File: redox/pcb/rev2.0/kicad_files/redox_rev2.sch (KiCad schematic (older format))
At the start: 144 parts, among them J1 AVR-ISP-6, J2 OLED-SSD1306, K1 KEYSW, K10 KEYSW, K11 KEYSW, K12 KEYSW, K13 KEYSW, K14 KEYSW, K15 KEYSW, K16 KEYSW, K17 KEYSW, K18 KEYSW, K19 KEYSW, K2 KEYSW, K20 KEYSW, K21 KEYSW, K22 KEYSW, K23 KEYSW, K24 KEYSW, K25 KEYSW, K26 KEYSW, K27 KEYSW, K28 KEYSW, K29 KEYSW, K3 KEYSW, K30 KEYSW, K31 KEYSW, K32 KEYSW, K33 KEYSW, K34 KEYSW, K35 KEYSW, K4 KEYSW, K5 KEYSW, K6 KEYSW, K7 KEYSW, K8 KEYSW, K9 KEYSW, Q1 2N7002, U1 PRTR5V0U2X, U2 ATmega32U4-MU, Y1 16Mhz

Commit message: PCB Routing in progress
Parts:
- added USB2: HRO-TYPE-C-31-M-12, Keebio-Parts:HRO-TYPE-C-31-M-12-Assembly, symbol Type-C:HRO-TYPE-C-31-M-12
- C5: footprint Keebio-Parts:C_0603 -> Capacitor_Tantalum_SMD:CP_EIA-3216-12_Kemet-S_Pad1.58x1.35mm_HandSolder; symbol Device:C_Small -> Device:CP1
- D1, D10, D11, D12, D13, D14, D15, D16, D17, D18, D19, D2, D20, D21, D22, D23, D24, D25, D26, D27, D28, D29, D3, D30, D31, D32, D33, D34, D35, D4, D5, D6, D7, D8, D9: footprint redox_footprints:Diode_SOD123 -> redox_footprints:D_0805_dualsided
- F1: footprint Keebio-Parts:Fuse_0805 -> Fuse:Fuse_1206_3216Metric_Pad1.42x1.75mm_HandSolder
- K11: footprint redox_footprints:Mx_Alps_125-dualside_with_LED -> redox_footprints:Mx_Alps_100-dualside_with_LED
- R10, R11, R12, R13, R14, R15, R16, R17, R18, R19, R20, R21, R22, R23, R24, R25, R26, R27, R28, R29, R30, R31, R32, R33, R34, R35, R36, R37, R38, R39, R40, R41, R42, R43, R44: footprint Keebio-Parts:Resistor-Compact -> redox_footprints:R_0805_dualsided
- U2: value ATmega32U4-MU -> ATmega32U4; symbol Voyager60-rescue:ATmega32U4-MU-MCU_Microchip_ATmega -> ATmega32U4:ATMEGA32U4
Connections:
- net labels added: XTAL1, XTAL2
- wire segments 509 -> 505
- no-connect marks 8 -> 10
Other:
- moved on the sheet: C1, C2, C3, C4, C6, C7, F1, H1, H2, H3, H4, J1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

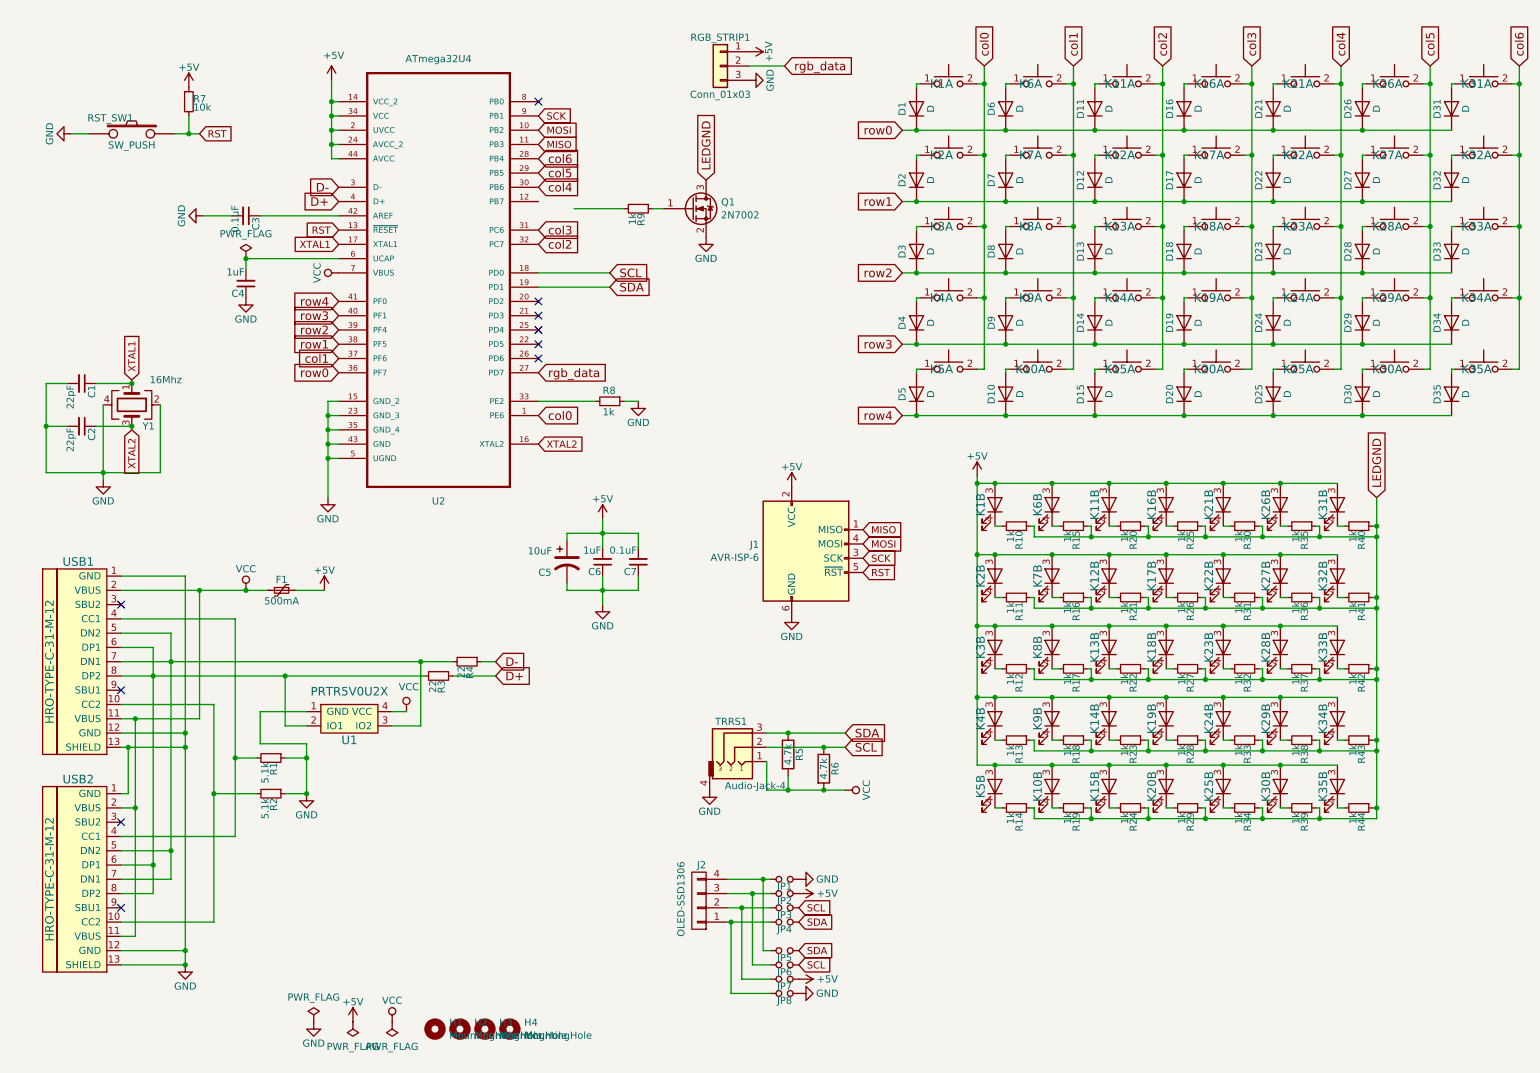
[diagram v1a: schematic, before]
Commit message: Create dual sided usb
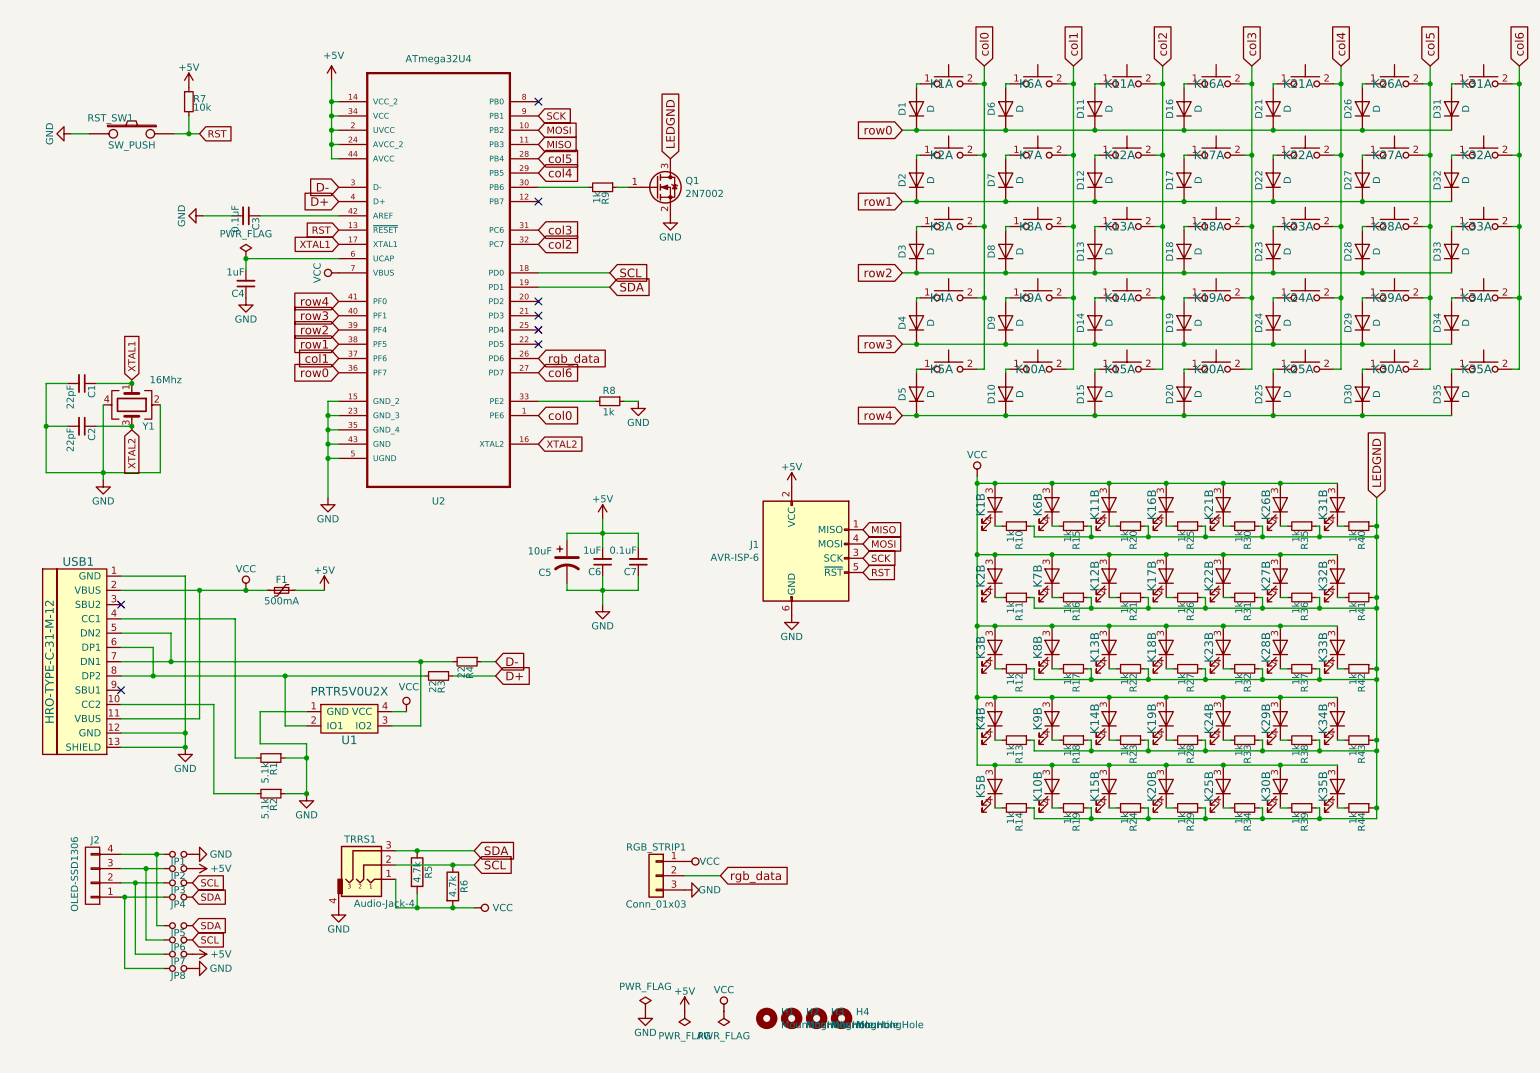
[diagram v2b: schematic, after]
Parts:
- removed USB2: HRO-TYPE-C-31-M-12, Keebio-Parts:HRO-TYPE-C-31-M-12-Assembly, symbol Type-C:HRO-TYPE-C-31-M-12
- USB1: footprint Keebio-Parts:HRO-TYPE-C-31-M-12-Assembly -> redox_footprints:HRO-TYPE-C-31-M-12-Assembly_dualsided
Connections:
- net +5V: no longer K1.3, K10.3, K11.3, K12.3, K13.3, K14.3, K15.3, K16.3, K17.3, K18.3, K19.3, K2.3, K20.3, K21.3, K22.3, K23.3, K24.3, K25.3, K26.3, K27.3, K28.3, K29.3, K3.3, K30.3, K31.3, K32.3, K33.3, K34.3, K35.3, K4.3, K5.3, K6.3, K7.3, K8.3, K9.3, RGB_STRIP1.1 (Pin_1)
- net VCC: now also K1.3, K10.3, K11.3, K12.3, K13.3, K14.3, K15.3, K16.3, K17.3, K18.3, K19.3, K2.3, K20.3, K21.3, K22.3, K23.3, K24.3, K25.3, K26.3, K27.3, K28.3, K29.3, K3.3, K30.3, K31.3, K32.3, K33.3, K34.3, K35.3, K4.3, K5.3, K6.3, K7.3, K8.3, K9.3, RGB_STRIP1.1 (Pin_1)
- net col4: now also U2.29 (PB5); no longer U2.30 (PB6)
- net col5: now also U2.28 (PB4); no longer U2.29 (PB5)
- net col6: now also U2.27 (PD7); no longer U2.28 (PB4)
- net rgb_data: now also U2.26 (PD6); no longer U2.27 (PD7)
- net at R9.2: now also U2.30 (PB6)
- no-connect marks 10 -> 8
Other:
- moved on the sheet: H1, H2, H3, H4, J2, JP1, JP2, JP3, JP4, JP5, JP6, JP7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

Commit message: Routing almost finished
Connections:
- net col4: now also U2.30 (PB6); no longer U2.29 (PB5)
- net col5: now also U2.29 (PB5); no longer U2.28 (PB4)
- net rgb_data: now also U2.28 (PB4); no longer U2.26 (PD6)
- net at R9.2: now also U2.26 (PD6); no longer U2.30 (PB6)
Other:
- moved on the sheet: Q1, R9
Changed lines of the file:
@@
 	-1   0    0    -1
 $EndComp
-Text GLabel 4675 2325 2    60   Input ~ 0
+Text GLabel 4175 2325 2    60   Input ~ 0
 SCL
-Text GLabel 4675 2425 2    60   Input ~ 0
+Text GLabel 4175 2425 2    60   Input ~ 0
 SDA
-Wire Wire Line
-	4675 2425 4175 2425
-Wire Wire Line
-	4675 2325 4175 2325
 Text GLabel 4175 3325 2    60   Input ~ 0
 col0
@@
 Text GLabel 4175 2025 2    60   Input ~ 0
 col3
-Text GLabel 4175 1625 2    60   Input ~ 0
+Text GLabel 4175 1725 2    60   Input ~ 0
 col4
-Text GLabel 4175 1525 2    60   Input ~ 0
+Text GLabel 4175 1625 2    60   Input ~ 0
 col5
 Text GLabel 4175 3025 2    60   Input ~ 0
@@
 Text GLabel 2775 2525 0    60   Input ~ 0
 row4
-Text GLabel 4175 2925 2    60   Input ~ 0
+Text GLabel 4175 1525 2    60   Input ~ 0
 rgb_data
 $Comp
@@
 L Device:R_Small R?
 U 1 1 5EDAEC9D
-P 4625 1725
+P 4825 2925
 AR Path="/5EAF3E37/5EDAEC9D" Ref="R?"  Part="1"
 AR Path="/5EDAEC9D" Ref="R9"  Part="1"
-F 0 "R9" H 4655 1745 50  0000 L CNN
-F 1 "1k" H 4655 1685 50  0000 L CNN
-F 2 "Keebio-Parts:R_0603" H 4625 1725 50  0001 C CNN
-F 3 "" H 4625 1725 50  0001 C CNN
-	1    4625 1725
+F 0 "R9" H 4855 2945 50  0000 L CNN
+F 1 "1k" H 4855 2885 50  0000 L CNN
+F 2 "Keebio-Parts:R_0603" H 4825 2925 50  0001 C CNN
+F 3 "" H 4825 2925 50  0001 C CNN
+	1    4825 2925
 	0    1    1    0
 $EndComp
-Text GLabel 5100 1525 1    60   Input ~ 0
+Text GLabel 5300 2725 1    60   Input ~ 0
 LEDGND
 $Comp
 L power:GND #PWR?
 U 1 1 5EDAECA4
-P 5100 1925
+P 5300 3125
 AR Path="/5EAF3E37/5EDAECA4" Ref="#PWR?"  Part="1"
 AR Path="/5EDAECA4" Ref="#PWR022"  Part="1"
-F 0 "#PWR022" H 5100 1675 50  0001 C CNN
-F 1 "GND" H 5100 1775 50  0000 C CNN
-F 2 "" H 5100 1925 50  0001 C CNN
-F 3 "" H 5100 1925 50  0001 C CNN
-	1    5100 1925
+F 0 "#PWR022" H 5300 2875 50  0001 C CNN
+F 1 "GND" H 5300 2975 50  0000 C CNN
+F 2 "" H 5300 3125 50  0001 C CNN
+F 3 "" H 5300 3125 50  0001 C CNN
+	1    5300 3125
 	1    0    0    -1
 $EndComp
@@
 	4875 3225 4775 3225
 Wire Wire Line
-	4525 1725 4175 1725
-Wire Wire Line
-	4725 1725 4800 1725
+	4925 2925 5000 2925
 Wire Wire Line
 	4375 4150 4625 4150
@@
 L Transistor_FET:2N7002 Q?
 U 1 1 5EDAED70
-P 5000 1725
+P 5200 2925
 AR Path="/5EAF3E37/5EDAED70" Ref="Q?"  Part="1"
 AR Path="/5EDAED70" Ref="Q1"  Part="1"
-F 0 "Q1" H 5205 1771 50  0000 L CNN
-F 1 "2N7002" H 5205 1680 50  0000 L CNN
-F 2 "Package_TO_SOT_SMD:SOT-23" H 5200 1650 50  0001 L CIN
-F 3 "https://www.fairchildsemi.com/datasheets/2N/2N7002.pdf" H 5000 1725 50  0001 L CNN
-	1    5000 1725
+F 0 "Q1" H 5405 2971 50  0000 L CNN
+F 1 "2N7002" H 5405 2880 50  0000 L CNN
+F 2 "Package_TO_SOT_SMD:SOT-23" H 5400 2850 50  0001 L CIN
+F 3 "https://www.fairchildsemi.com/datasheets/2N/2N7002.pdf" H 5200 2925 50  0001 L CNN
+	1    5200 2925
 	1    0    0    -1
 $EndComp
@@
 P 7250 3750
 AR Path="/5EAF3E37/5F2FCD0A" Ref="#PWR?"  Part="1"
-AR Path="/5F2FCD0A" Ref="#PWR?"  Part="1"
-F 0 "#PWR?" H 7250 3600 50  0001 C CNN
+AR Path="/5F2FCD0A" Ref="#PWR0106"  Part="1"
+F 0 "#PWR0106" H 7250 3600 50  0001 C CNN
 F 1 "VCC" H 7250 3900 50  0000 C CNN
 F 2 "" H 7250 3750 50  0001 C CNN
@@
 	1    0    0    -1
 $EndComp
+Wire Wire Line
+	4725 2925 4175 2925
 $EndSCHEMATC

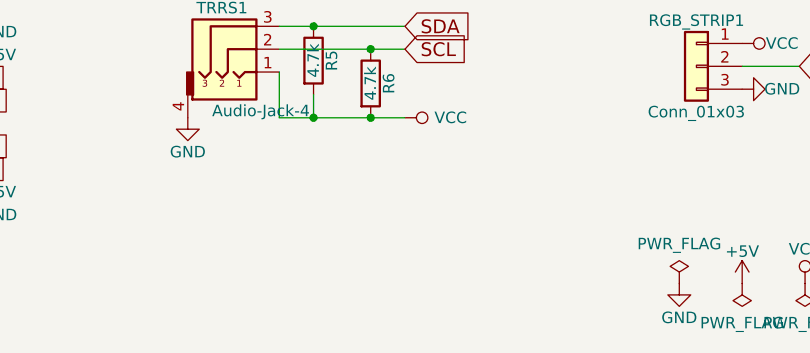
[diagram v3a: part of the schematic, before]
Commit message: Add OSH logo
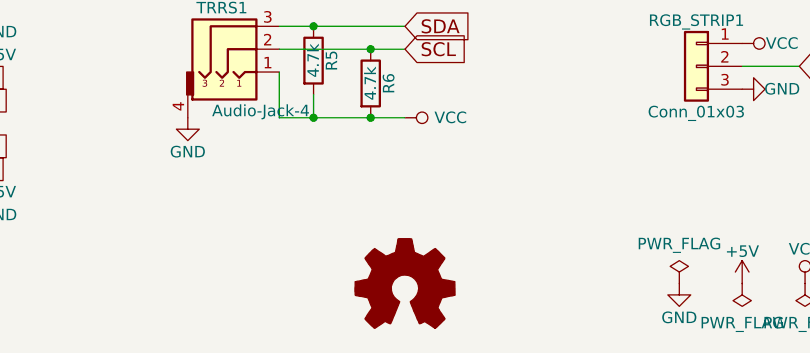
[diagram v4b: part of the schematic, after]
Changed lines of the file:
@@
 Wire Wire Line
 	4725 2925 4175 2925
+$Comp
+L Graphic:Logo_Open_Hardware_Small #LOGO1
+U 1 1 6041354B
+P 3725 7525
+F 0 "#LOGO1" H 3725 7800 50  0001 C CNN
+F 1 "Logo_Open_Hardware_Small" H 3725 7300 50  0001 C CNN
+F 2 "" H 3725 7525 50  0001 C CNN
+F 3 "~" H 3725 7525 50  0001 C CNN
+	1    3725 7525
+	1    0    0    -1
+$EndComp
 $EndSCHEMATC

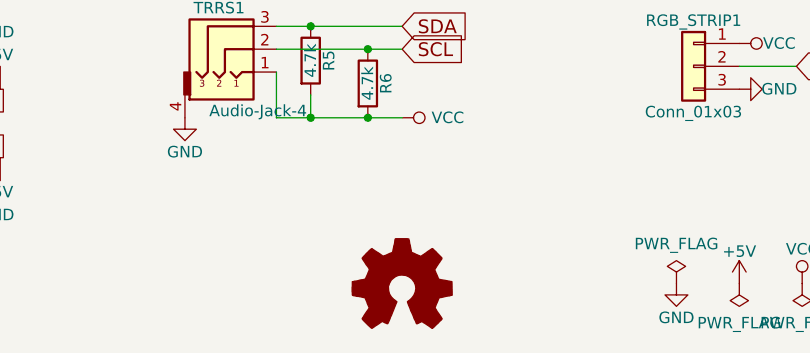
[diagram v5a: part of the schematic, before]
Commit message: Change ATùega32u4-MU QFN-44 footprint from standard library
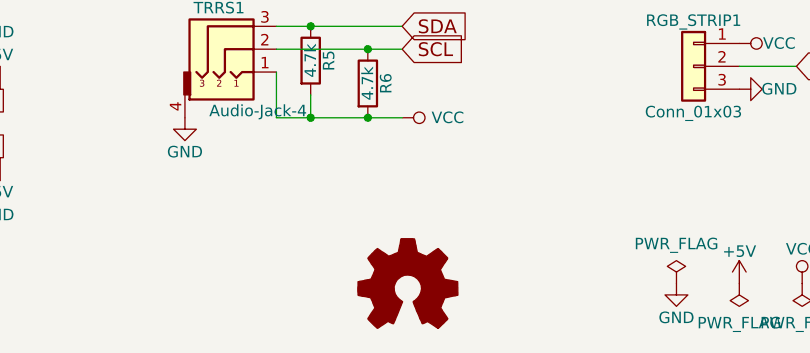
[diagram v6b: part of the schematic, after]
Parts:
- U2: footprint Keebio-Parts:QFN-44-1EP_7x7mm_Pitch0.5mm -> Package_DFN_QFN:QFN-44-1EP_7x7mm_P0.5mm_EP5.2x5.2mm_ThermalVias
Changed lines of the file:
@@
 F 0 "U2" H 3475 525 50  0000 C CNN
 F 1 "ATmega32U4" H 3475 3625 50  0000 C CNN
-F 2 "Keebio-Parts:QFN-44-1EP_7x7mm_Pitch0.5mm" H 3475 2225 50  0001 C CIN
+F 2 "Package_DFN_QFN:QFN-44-1EP_7x7mm_P0.5mm_EP5.2x5.2mm_ThermalVias" H 3475 2225 50  0001 C CIN
 F 3 "http://ww1.microchip.com/downloads/en/DeviceDoc/Atmel-7766-8-bit-AVR-ATmega16U4-32U4_Datasheet.pdf" H 3475 2225 50  0001 C CNN
 	1    3475 2225
@@
 L Graphic:Logo_Open_Hardware_Small #LOGO1
 U 1 1 6041354B
-P 3725 7525
-F 0 "#LOGO1" H 3725 7800 50  0001 C CNN
-F 1 "Logo_Open_Hardware_Small" H 3725 7300 50  0001 C CNN
-F 2 "" H 3725 7525 50  0001 C CNN
-F 3 "~" H 3725 7525 50  0001 C CNN
-	1    3725 7525
-	1    0    0    -1
-$EndComp
+P 3750 7525
+F 0 "#LOGO1" H 3750 7800 50  0001 C CNN
+F 1 "Logo_Open_Hardware_Small" H 3750 7300 50  0001 C CNN
+F 2 "" H 3750 7525 50  0001 C CNN
+F 3 "~" H 3750 7525 50  0001 C CNN
+	1    3750 7525
+	1    0    0    -1
+$EndComp
